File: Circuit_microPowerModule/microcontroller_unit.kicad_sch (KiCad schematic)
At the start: 69 parts, among them J201 USB_C_Receptacle_USB2.0, J202 Debug, SW201 KMR2, U201 W25Q128JVS, U202 RP2040, Y201 12MHz

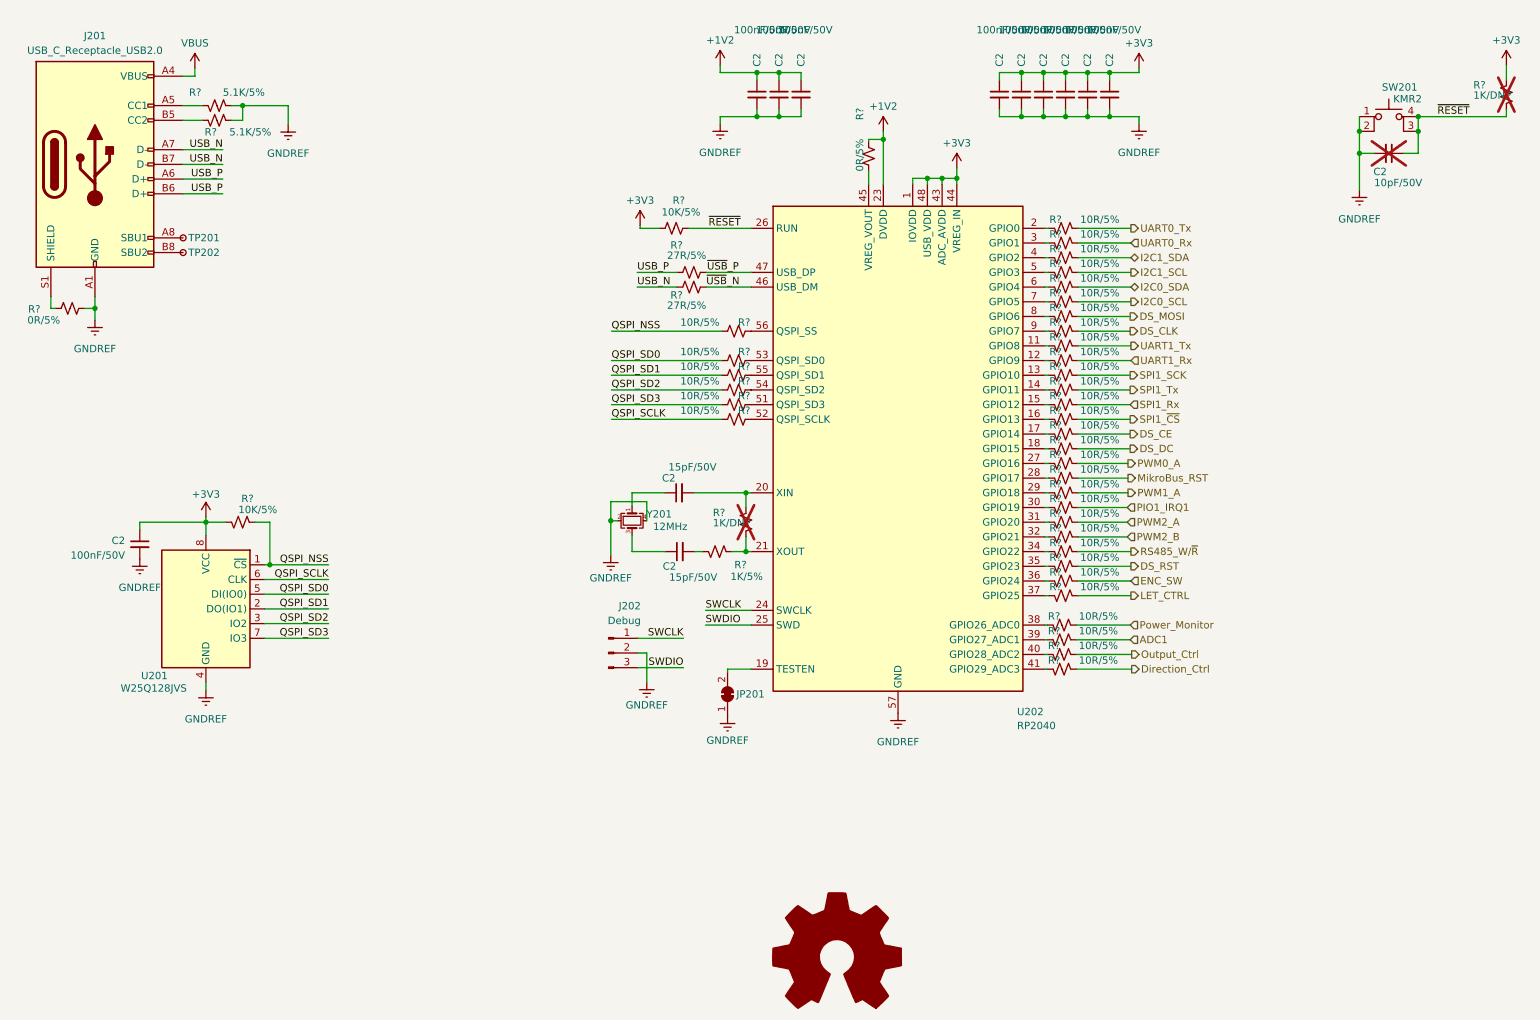
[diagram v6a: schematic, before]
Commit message: modify ERC warning
modify OPA, TVS-Diode, Cap
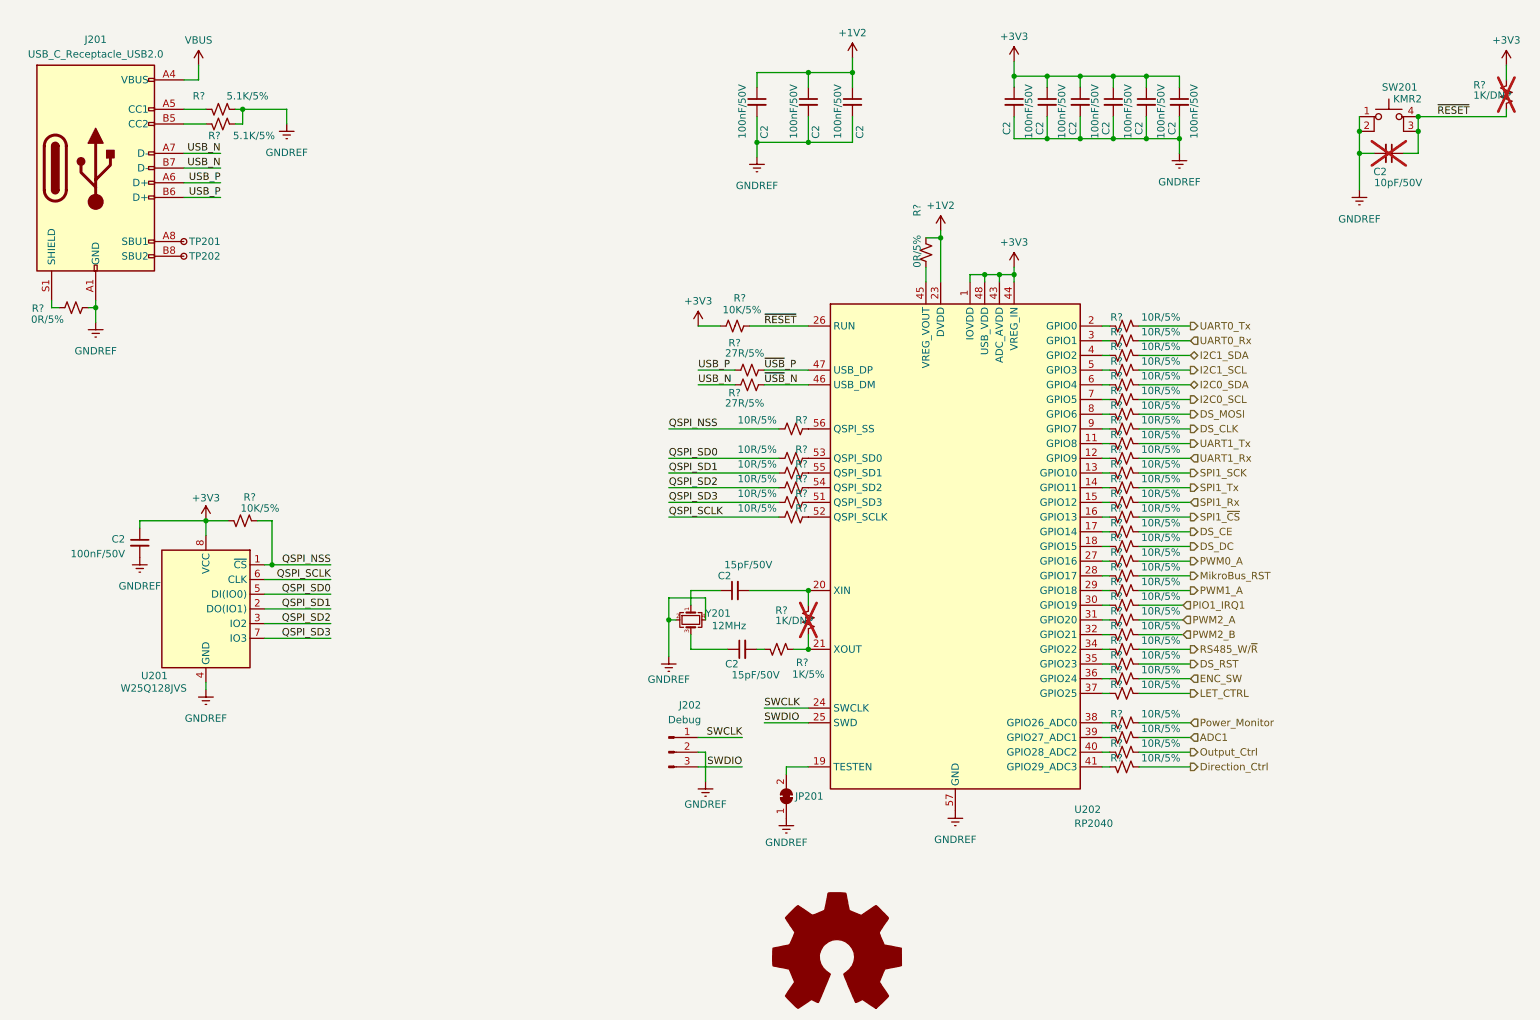
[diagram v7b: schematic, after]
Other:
- moved on the sheet: C2, J201, J202, JP201, R?, TP201, TP202, U202, Y201

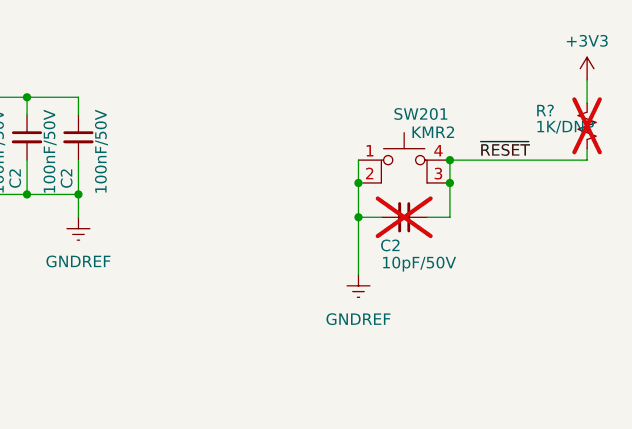
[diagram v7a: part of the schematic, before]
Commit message: start pcb layout
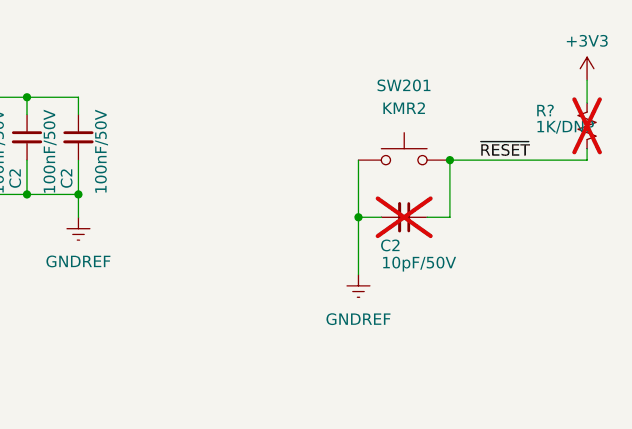
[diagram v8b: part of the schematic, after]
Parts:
- removed SW201: KMR2, Button_Switch_SMD:SW_Push_1P1T_NO_CK_KMR2, symbol Switch:SW_MEC_5E
- added SW201: KMR2, Button_Switch_SMD:SW_Push_1P1T_NO_CK_KMR2, symbol Switch:SW_Push
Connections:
- net GNDREF: now also SW201.1
- net ~{RESET}: now also SW201.2
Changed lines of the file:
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@@
   (junction (at 154.94 113.665) (diameter 0) (color 0 0 0 0)
   )
-  (junction (at 250.19 34.29) (diameter 0) (color 0 0 0 0)
-  )
   (junction (at 219.075 35.56) (diameter 0) (color 0 0 0 0)
   )
@@
   (junction (at 207.645 24.765) (diameter 0) (color 0 0 0 0)
   )
+  (junction (at 260.35 31.75) (diameter 0) (color 0 0 0 0)
+  )
   (junction (at 213.36 24.765) (diameter 0) (color 0 0 0 0)
   )
@@
   (junction (at 201.93 24.765) (diameter 0) (color 0 0 0 0)
   )
-  (junction (at 260.35 31.75) (diameter 0) (color 0 0 0 0)
-  )
   (junction (at 31.75 64.77) (diameter 0) (color 0 0 0 0)
   )
@@
   (junction (at 190.5 59.055) (diameter 0) (color 0 0 0 0)
   )
-  (junction (at 260.35 34.29) (diameter 0) (color 0 0 0 0)
-  )
   (junction (at 187.96 59.055) (diameter 0) (color 0 0 0 0)
   )
@@
     (stroke (width 0) (type default))
   )
-  (wire (pts (xy 250.19 38.1) (xy 250.19 34.29))
+  (wire (pts (xy 250.19 31.75) (xy 250.19 38.1))
     (stroke (width 0) (type default))
   )
@@
     (stroke (width 0) (type default))
   )
-  (wire (pts (xy 260.35 38.1) (xy 260.35 34.29))
+  (wire (pts (xy 260.35 31.75) (xy 260.35 38.1))
     (stroke (width 0) (type default))
   )
@@
     (stroke (width 0) (type default))
   )
-  (wire (pts (xy 260.35 31.75) (xy 260.35 34.29))
-    (stroke (width 0) (type default))
-  )
   (wire (pts (xy 212.09 100.965) (xy 220.98 100.965))
     (stroke (width 0) (type default))
@@
     (stroke (width 0) (type default))
   )
-  (wire (pts (xy 250.19 31.75) (xy 250.19 34.29))
-    (stroke (width 0) (type default))
-  )
   (wire (pts (xy 30.48 64.77) (xy 31.75 64.77))
     (stroke (width 0) (type default))
@@
     )
   )
-  (symbol (lib_id "Switch:SW_MEC_5E") (at 255.27 34.29 0) (unit 1)
-    (in_bom yes) (on_board yes) (dnp no)
-    (property "Reference" "SW201" (at 260.223 26.67 0)
-      (effects (font (size 1.27 1.27)) (justify right))
+  (symbol (lib_id "Switch:SW_Push") (at 255.27 31.75 0) (unit 1)
+    (in_bom yes) (on_board yes) (dnp no) (fields_autoplaced)
+    (property "Reference" "SW201" (at 255.27 23.495 0)
+      (effects (font (size 1.27 1.27)))
     )
-    (property "Value" "KMR2" (at 260.985 28.702 0)
-      (effects (font (size 1.27 1.27)) (justify right))
+    (property "Value" "KMR2" (at 255.27 26.035 0)
+      (effects (font (size 1.27 1.27)))
     )
     (property "Footprint" "Button_Switch_SMD:SW_Push_1P1T_NO_CK_KMR2" (at 255.27 26.67 0)
@@
     (pin "1")
     (pin "2")
-    (pin "3")
-    (pin "4")
     (instances
       (project "micro-PowerModule"
